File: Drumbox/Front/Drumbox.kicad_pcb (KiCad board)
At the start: 2 copper layers, 286 x 133 mm, 117 parts, among them J1 Conn_01x04_Male, J10 Bass OUT, J11 LBonga OUT, J12 Conn_01x04_Female, J13 Conn_01x04_Male, J14 Conn_01x04_Female, J15 Conn_01x04_Male, J16 HBonga OUT, J17 Clave OUT, J18 Conn_01x03_Female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

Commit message: create gerber for drumbox
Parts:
- removed C1, C13: 150nF, Capacitor_THT:C_Disc_D7.0mm_W2.5mm_P5.00mm
- removed C10, C9: 12nF, Capacitor_THT:C_Disc_D7.0mm_W2.5mm_P5.00mm
- removed C11, C12: 1.5nF, Capacitor_THT:C_Disc_D7.0mm_W2.5mm_P5.00mm
- removed C14, C2: 33nF, Capacitor_THT:C_Disc_D7.0mm_W2.5mm_P5.00mm
- removed C15, C3: 39nF, Capacitor_THT:C_Disc_D7.0mm_W2.5mm_P5.00mm
- removed C16: 4.7nF, Capacitor_THT:C_Disc_D7.0mm_W2.5mm_P5.00mm
- removed C17, C18: 10µ, Capacitor_THT:CP_Radial_D5.0mm_P2.00mm
- removed C19, C20, C23, C24: .1µF, Capacitor_THT:C_Disc_D7.0mm_W2.5mm_P5.00mm
- removed C27, C28: 100n, Capacitor_THT:CP_Radial_D5.0mm_P2.00mm
- removed C4: 56nF, Capacitor_THT:C_Disc_D7.0mm_W2.5mm_P5.00mm
- removed C5, C6: 47nF, Capacitor_THT:C_Disc_D7.0mm_W2.5mm_P5.00mm
- removed C7, C8: 10nF, Capacitor_THT:C_Disc_D7.0mm_W2.5mm_P5.00mm
- removed D1, D2, D3, D4: 1N4148, Diode_THT:D_DO-35_SOD27_P7.62mm_Horizontal
- removed D5: LED-12V, LED_THT:LED_D4.0mm
- removed D6: LED1, LED_THT:LED_D4.0mm
- removed D7: LED2, LED_THT:LED_D4.0mm
- removed D8: LED3, LED_THT:LED_D4.0mm
- removed D9: LED4, LED_THT:LED_D4.0mm
- removed DECAY1, DECAY2, DECAY3, DECAY4: 470k, Potentiometer_THT:Potentiometer_Bourns_PTV09A-1_Single_Vertical
- removed FB1, FB2: 10R, Inductor_THT:L_Axial_L9.5mm_D4.0mm_P12.70mm_Horizontal_Fastron_SMCC
- removed J1, J13, J15, J3: Conn_01x04_Male, Connector_PinHeader_2.54mm:PinHeader_1x04_P2.54mm_Vertical
- removed J10: Bass OUT, Connector_Audio:Jack_3.5mm_QingPu_WQP-PJ398SM_Vertical_CircularHoles
- removed J11: LBonga OUT, Connector_Audio:Jack_3.5mm_QingPu_WQP-PJ398SM_Vertical_CircularHoles
- removed J12, J14, J2, J4: Conn_01x04_Female, Connector_PinSocket_2.54mm:PinSocket_1x04_P2.54mm_Vertical
- removed J16: HBonga OUT, Connector_Audio:Jack_3.5mm_QingPu_WQP-PJ398SM_Vertical_CircularHoles
- removed J17: Clave OUT, Connector_Audio:Jack_3.5mm_QingPu_WQP-PJ398SM_Vertical_CircularHoles
- removed J18: Conn_01x03_Female, Connector_PinSocket_2.54mm:PinSocket_1x03_P2.54mm_Vertical
- removed J19: Conn_01x03_Male, Connector_PinHeader_2.54mm:PinHeader_1x03_P2.54mm_Vertical
- removed J5: Power Input, Connector_PinHeader_2.54mm:PinHeader_2x05_P2.54mm_Vertical
- removed J6: Bass IN, Connector_Audio:Jack_3.5mm_QingPu_WQP-PJ398SM_Vertical_CircularHoles
- removed J7: LBonga IN, Connector_Audio:Jack_3.5mm_QingPu_WQP-PJ398SM_Vertical_CircularHoles
- removed J8: HBonga IN, Connector_Audio:Jack_3.5mm_QingPu_WQP-PJ398SM_Vertical_CircularHoles
- removed J9: Clave IN, Connector_Audio:Jack_3.5mm_QingPu_WQP-PJ398SM_Vertical_CircularHoles
- removed PITCH1, PITCH2, PITCH3, PITCH4, VOL1, VOL2, VOL3, VOL4: 10k, Potentiometer_THT:Potentiometer_Bourns_PTV09A-1_Single_Vertical
- removed Q1, Q2, Q3, Q4: 2N3904, Package_TO_SOT_THT:TO-92_Inline
- removed R1, R2, R3, R4: 150k, Resistor_THT:R_Axial_DIN0207_L6.3mm_D2.5mm_P10.16mm_Horizontal
- removed R10, R11, R12, R5, R6, R7, R8, R9: 68k, Resistor_THT:R_Axial_DIN0207_L6.3mm_D2.5mm_P10.16mm_Horizontal
- removed R13, R14, R15, R16: 27k, Resistor_THT:R_Axial_DIN0207_L6.3mm_D2.5mm_P10.16mm_Horizontal
- removed R17, R19, R21, R23: 12k, Resistor_THT:R_Axial_DIN0207_L6.3mm_D2.5mm_P10.16mm_Horizontal
- removed R18, R20, R22, R24, R30, R31, R32, R33: 47k, Resistor_THT:R_Axial_DIN0207_L6.3mm_D2.5mm_P10.16mm_Horizontal
- removed R25: 2.2k, Resistor_THT:R_Axial_DIN0207_L6.3mm_D2.5mm_P10.16mm_Horizontal
- removed R26, R27, R28, R29, R36, R37, R40, R41: 1k, Resistor_THT:R_Axial_DIN0207_L6.3mm_D2.5mm_P10.16mm_Horizontal
- removed R34, R35, R38, R39: 1M, Resistor_THT:R_Axial_DIN0207_L6.3mm_D2.5mm_P10.16mm_Horizontal
- removed U1: 4011, Package_DIP:DIP-14_W7.62mm_Socket
- removed U2: TL074, Package_DIP:DIP-14_W7.62mm_Socket
- moved ? 111.1 mm to (97.1, 156.2)
- moved ? 111.1 mm to (193.1, 156.2)
- moved REF** 111.1 mm to (193.1, 29.2)
- moved REF** 111.1 mm to (97.1, 29.2)
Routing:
- net +12V: track 256.9 -> 0.00 mm, vias 2 -> 0
- net O4: track 185.6 -> 0.00 mm
- net O1: track 156.9 -> 0.00 mm
- net O3: track 139.9 -> 0.00 mm
- net O2: track 135.7 -> 0.00 mm
- net PIOut4: track 119.4 -> 0.00 mm
- net In4: track 108.2 -> 0.00 mm
- net PIOut3: track 86.5 -> 0.00 mm
- net Net-(C9-Pad1): track 82.2 -> 0.00 mm, vias 1 -> 0
- net In3: track 79.7 -> 0.00 mm
- net Net-(C11-Pad1): track 76.8 -> 0.00 mm, vias 3 -> 0
- net Net-(C5-Pad1): track 76.1 -> 0.00 mm
- net Net-(C7-Pad1): track 69.8 -> 0.00 mm
- net DEIn4: track 68.2 -> 0.00 mm
- net DEIn1: track 67.8 -> 0.00 mm
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- removed copper zone on B.Cu, net GND
- removed copper zone on F.Cu, net GND
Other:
- board size 286 x 133 mm -> 120 x 133 mm
- board text removed: "24HP"
- board text removed: "8HP"
- board text removed: "Drumbox V1.0 BleepSound 2022"
- board text removed: "board 1/2"
- board text removed: "board 2/2"

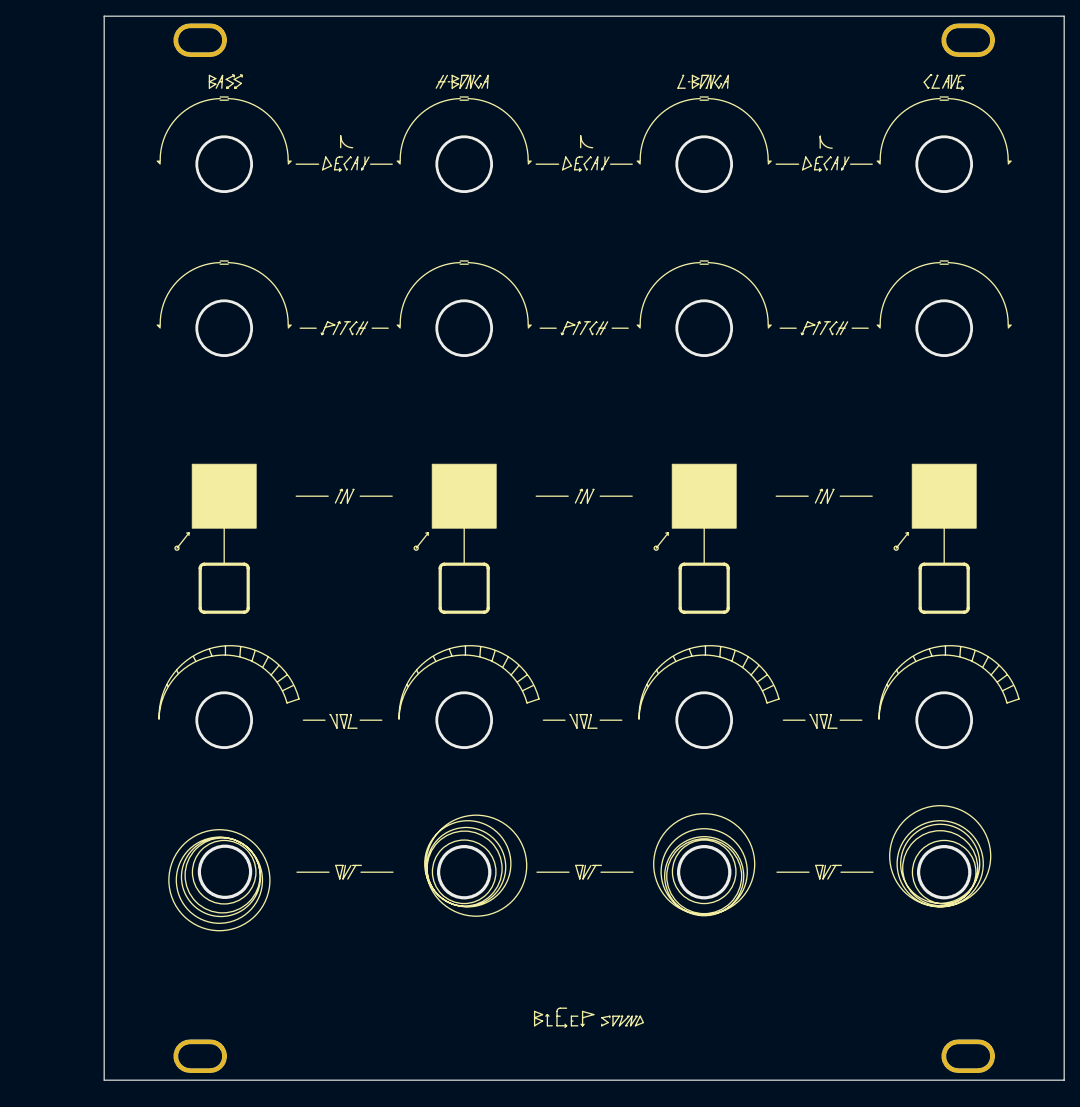
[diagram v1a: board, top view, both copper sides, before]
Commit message: update drumbox with hole size
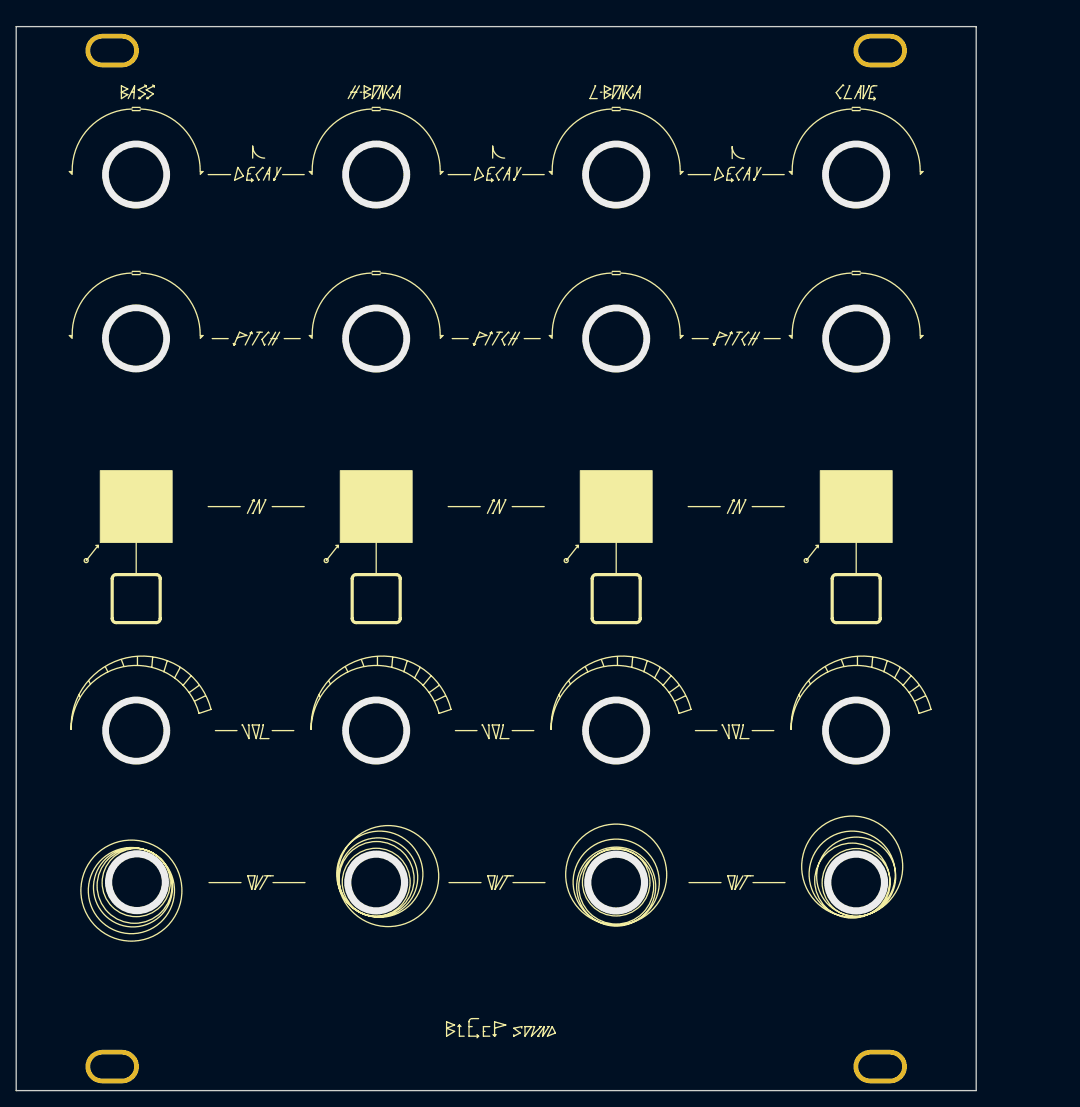
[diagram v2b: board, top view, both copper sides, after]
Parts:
- moved ? 11.1 mm to (86.1, 157.5)
- moved ? 11.1 mm to (182.1, 157.5)
- moved REF** 11.1 mm to (182.1, 30.5)
- moved REF** 11.1 mm to (86.1, 30.5)

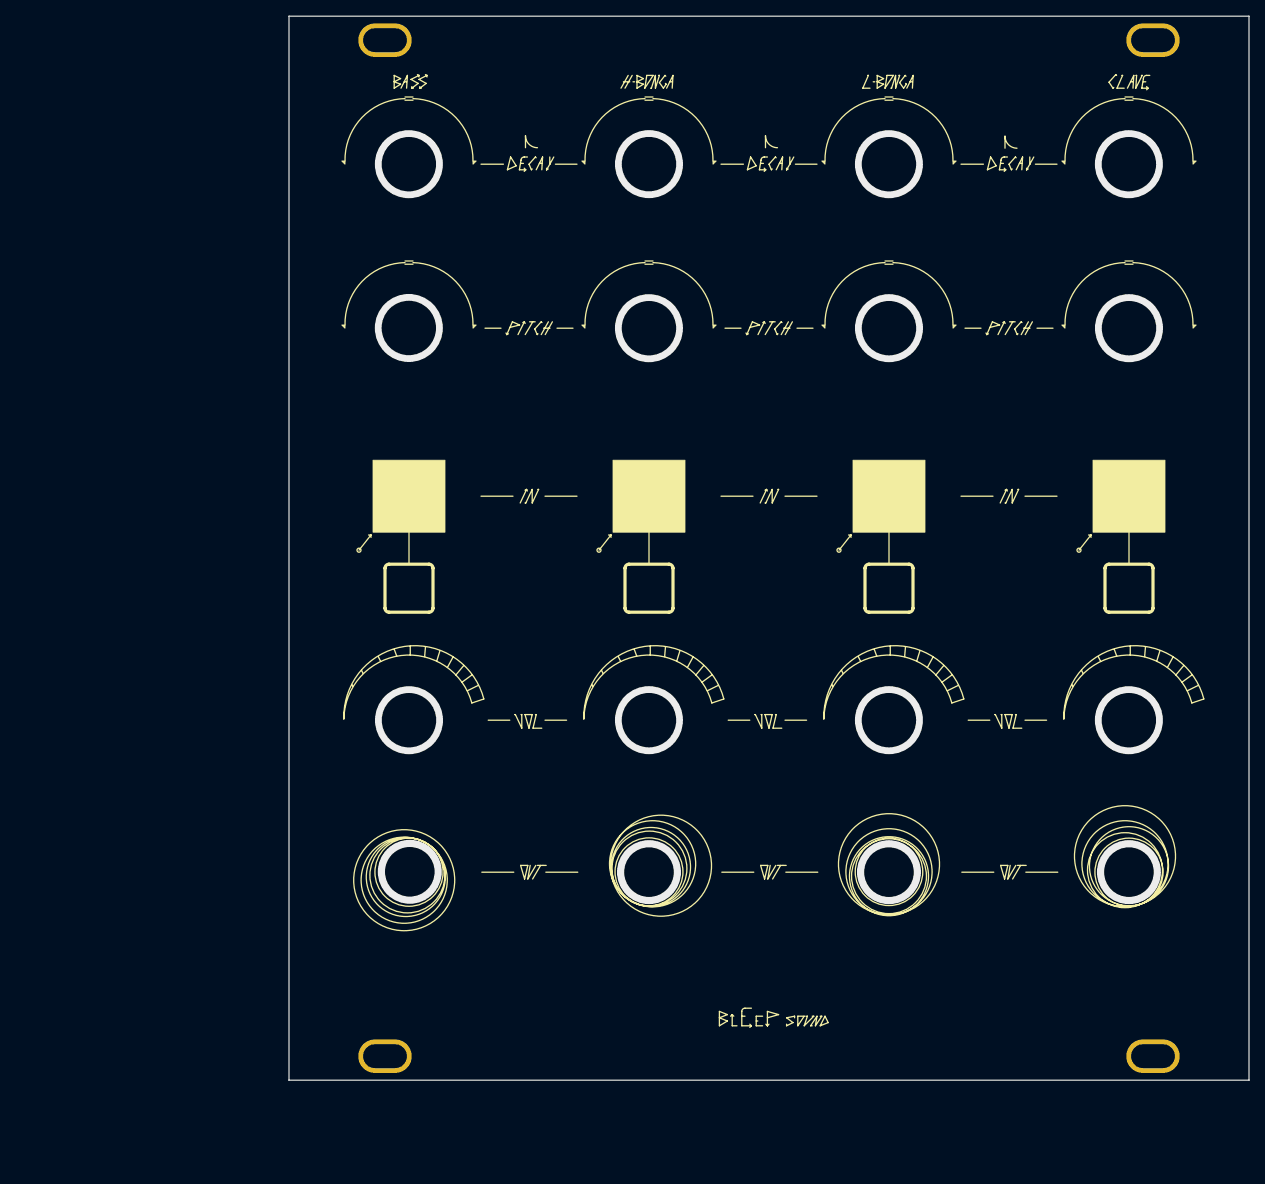
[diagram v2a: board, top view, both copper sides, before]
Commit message: update front panel size
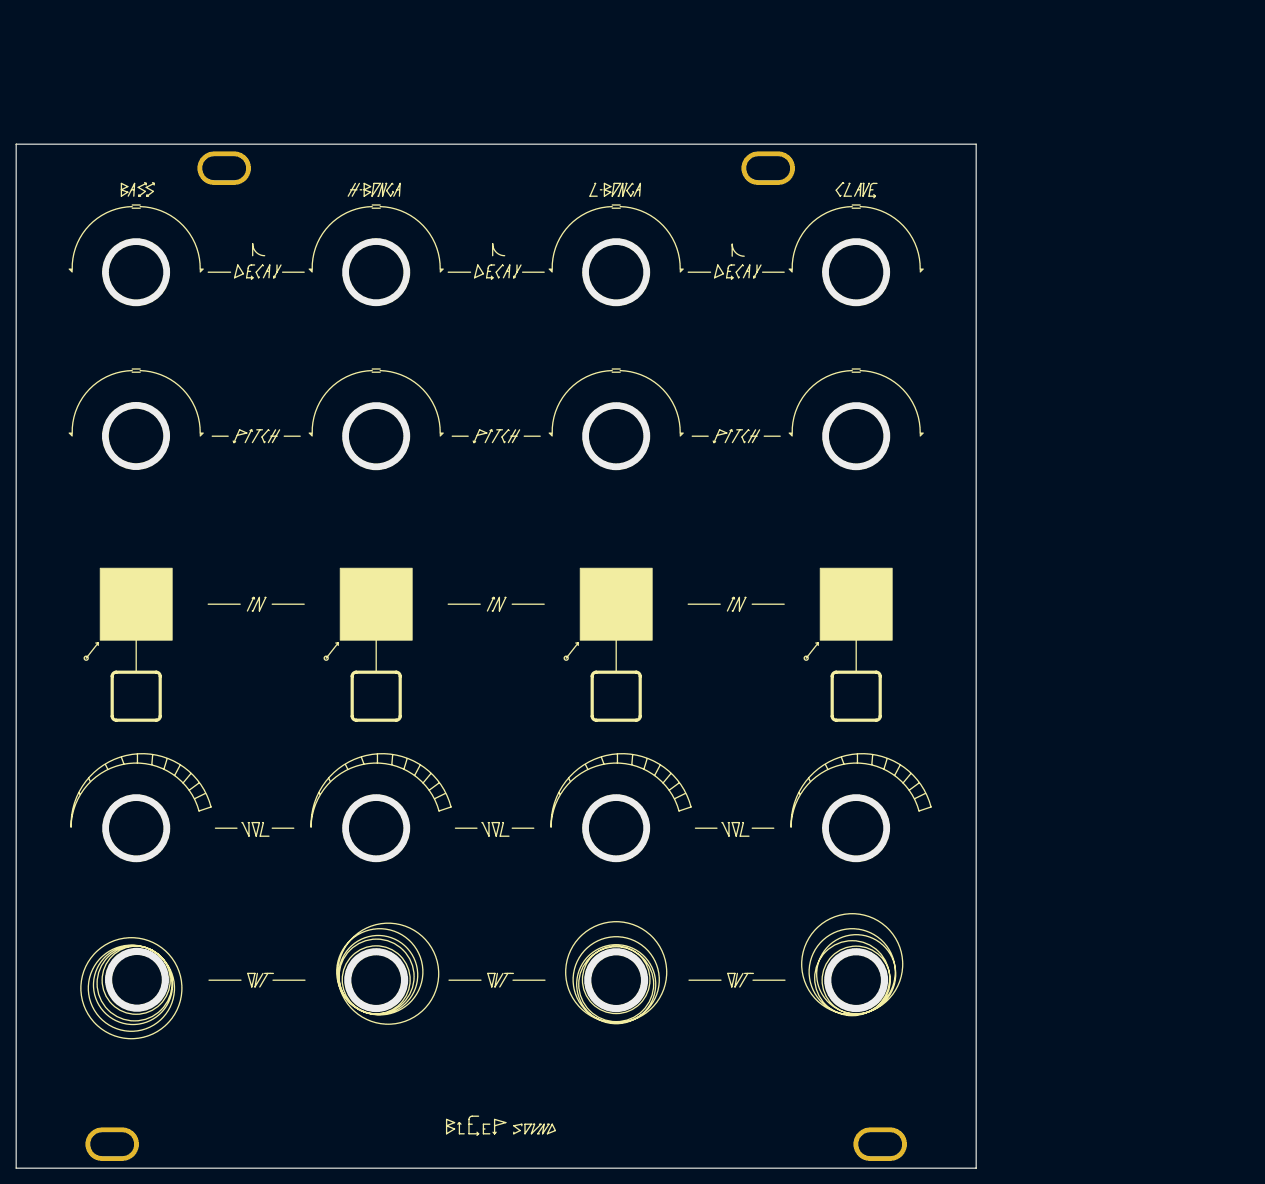
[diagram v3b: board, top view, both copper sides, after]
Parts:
- removed the ? at (86.1, 157.5)
- removed the ? at (182.1, 157.5)
- removed the REF** at (182.1, 30.5)
- removed the REF** at (86.1, 30.5)
- added ?: , , F.Cu at (52.0, 168.5)
- added ?: , , F.Cu at (148.0, 168.5)
- added REF**: Doepfer Mounting hole, Synth:Doepfer Mounting hole, F.Cu at (134.0, 46.5)
- added REF**: Doepfer Mounting hole, Synth:Doepfer Mounting hole, F.Cu at (66.0, 46.5)
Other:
- board size 120 x 133 mm -> 120 x 128 mm
